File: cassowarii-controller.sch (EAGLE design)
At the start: 17 parts, among them J1 Power, J2 2-PIN_2MM-H, J3 2-PIN_2MM-H, U1 ATTiny85

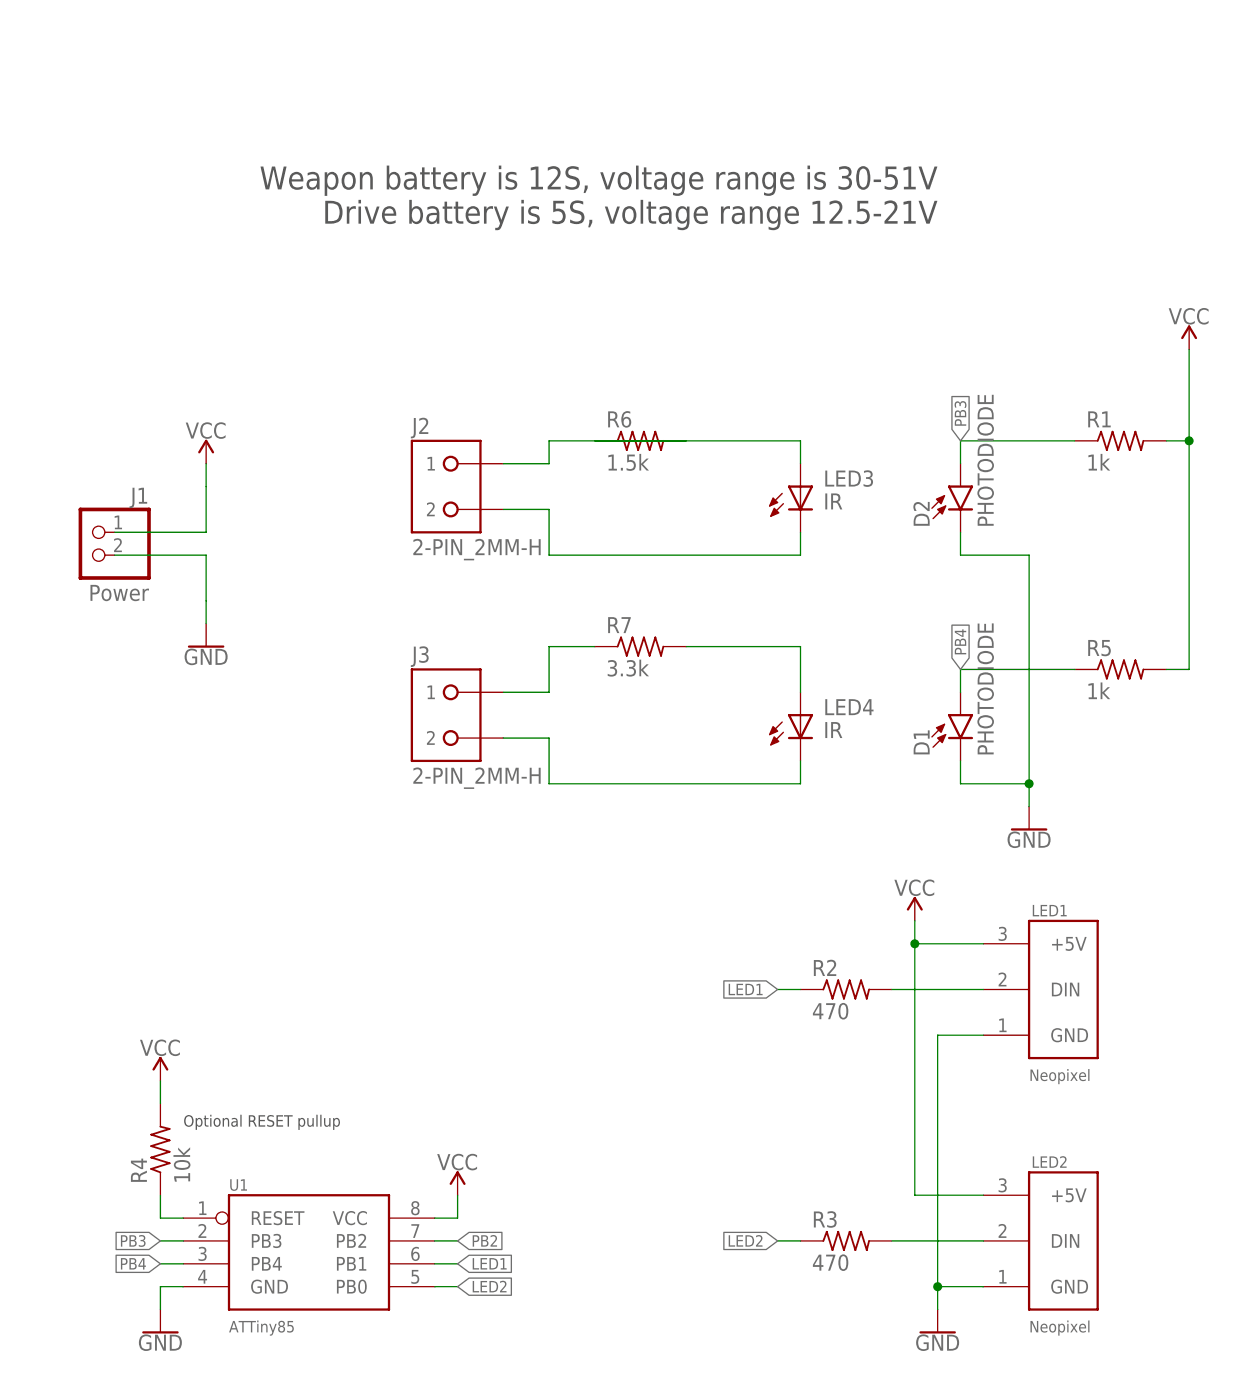
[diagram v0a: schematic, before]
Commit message: New version of Cassowarii controller with proper optoisolators
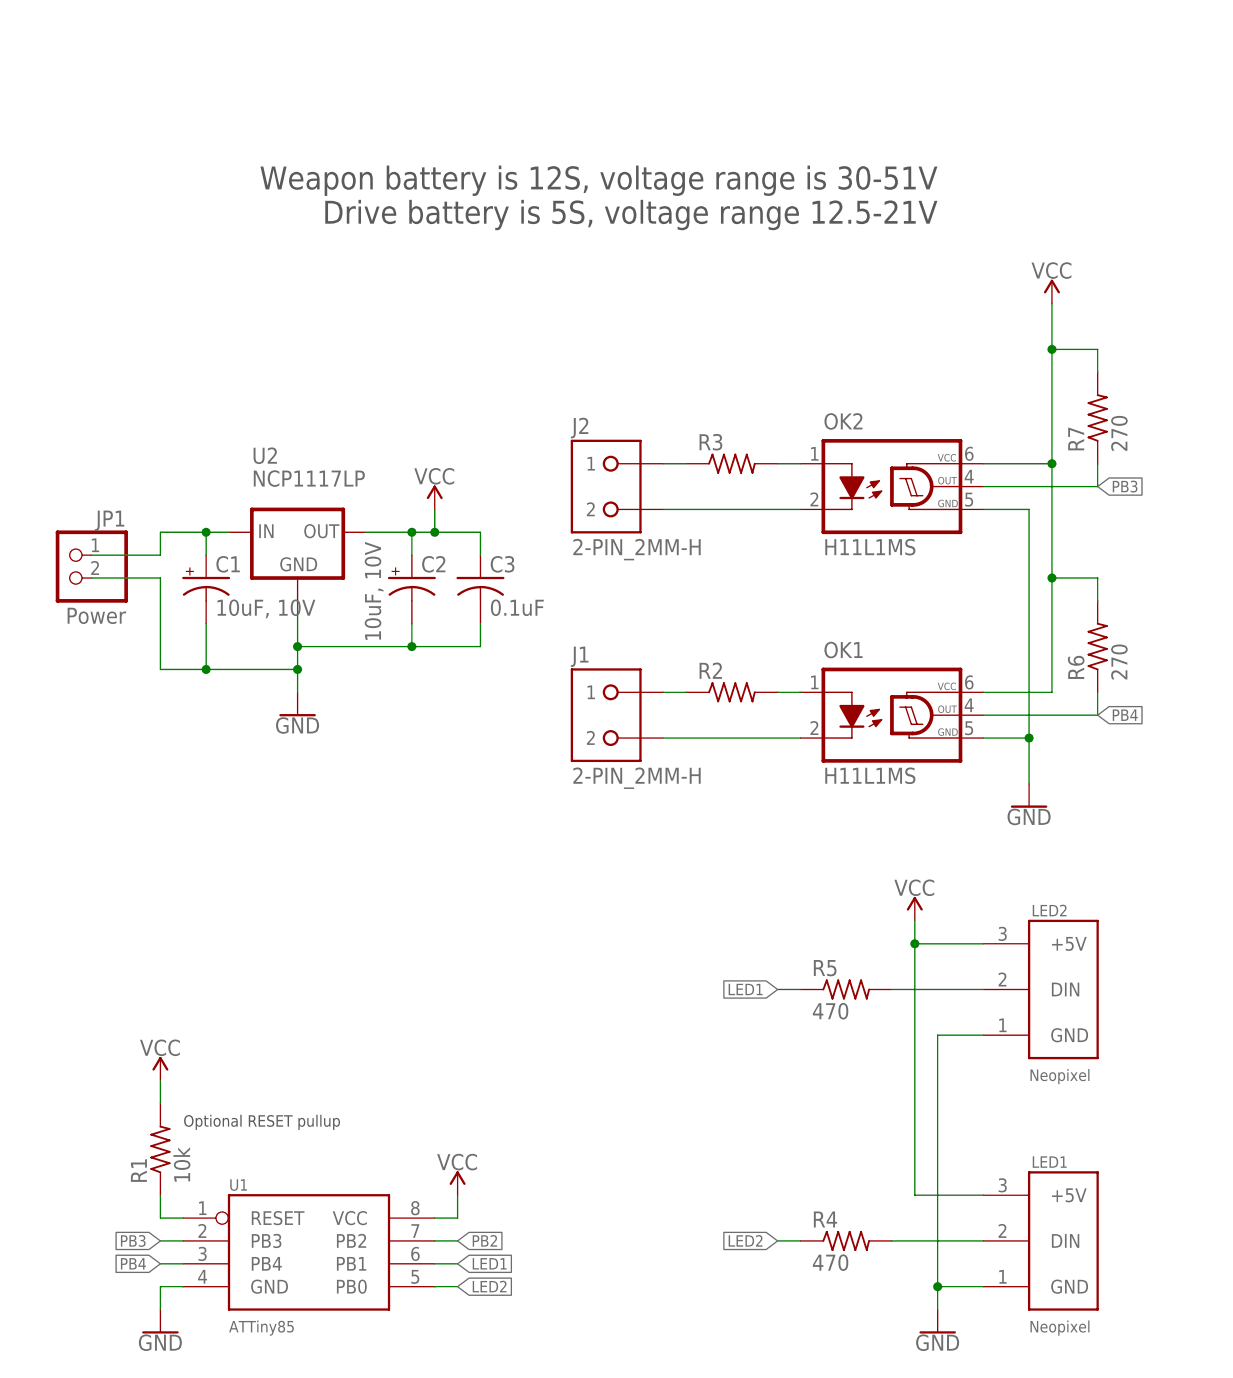
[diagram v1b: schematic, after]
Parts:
- removed D1, D2: PHOTODIODE, JoshCustom:PHOTODIODE
- removed J3: 2-PIN_2MM-H, RoboJackets-Connectors:2-PIN_2MM-H
- removed LED3, LED4: IR, JoshCustom:LED
- added C1, C2: 10uF, 10V, resistor:CPOL-USE1.8-4
- added C3: 0.1uF, resistor:C-USC0805
- added JP1: Power, pinhead:PINHD-1X2
- added OK1, OK2: H11L1MS, optocoupler:H11L1MS
- added U2: NCP1117LP, JoshCustom:NCP1117LP
- J1: value Power -> 2-PIN_2MM-H; device pinhead:PINHD-1X2 -> RoboJackets-Connectors:2-PIN_2MM-H
- R1: value 1k -> 10k
- R2, R3: value 470 -> (none); device resistor:R-US_R0805 -> resistor:R-US_0204/2V
- R4: value 10k -> 470
- R5: value 1k -> 470
- R6: value 1.5k -> 270; device resistor:R-US_0204/2V -> resistor:R-US_R0805
- R7: value 3.3k -> 270; device resistor:R-US_0204/2V -> resistor:R-US_R0805
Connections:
- removed net N$4: LED3.A, R6.1
- new net N$10: OK2.A, R3.2
- new net N$11: C1.+, JP1.1, U2.IN
- net GND: now also C1.-, C2.-, C3.2, JP1.2, OK1.GND, OK2.GND, U2.GND; no longer D1.C, D2.C, J1.2
- net LED1: now also R5.1; no longer R2.1
- net LED2: now also R4.1; no longer R3.1
- net N$1: now also LED1.DIN, R4.2; no longer LED2.DIN, R3.2
- net N$2: now also LED2.DIN, R5.2; no longer LED1.DIN, R2.2
- net N$3: now also R3.1; no longer R6.2
- net N$5: now also R1.1; no longer R4.1
- net N$6: now also OK2.C; no longer LED3.K
- net N$7: now also J1.1, R2.1; no longer J3.1, R7.1
- net N$8: now also OK1.A, R2.2; no longer LED4.A, R7.2
- net N$9: now also J1.2, OK1.C; no longer J3.2, LED4.K
- net PB3: now also OK2.OUT, R7.1; no longer D2.A, R1.1
- net PB4: now also OK1.OUT, R6.1; no longer D1.A, R5.1
- net VCC: now also C2.+, C3.1, OK1.VCC, OK2.VCC, R6.2, R7.2, U2.OUT; no longer J1.1, R4.2, R5.2
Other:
- moved on the sheet: J1, J2, LED1, LED2, R1, R2, R3, R4, R5, R6, R7

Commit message: Redesign Cassowarii controller to use SOIC ATTiny85
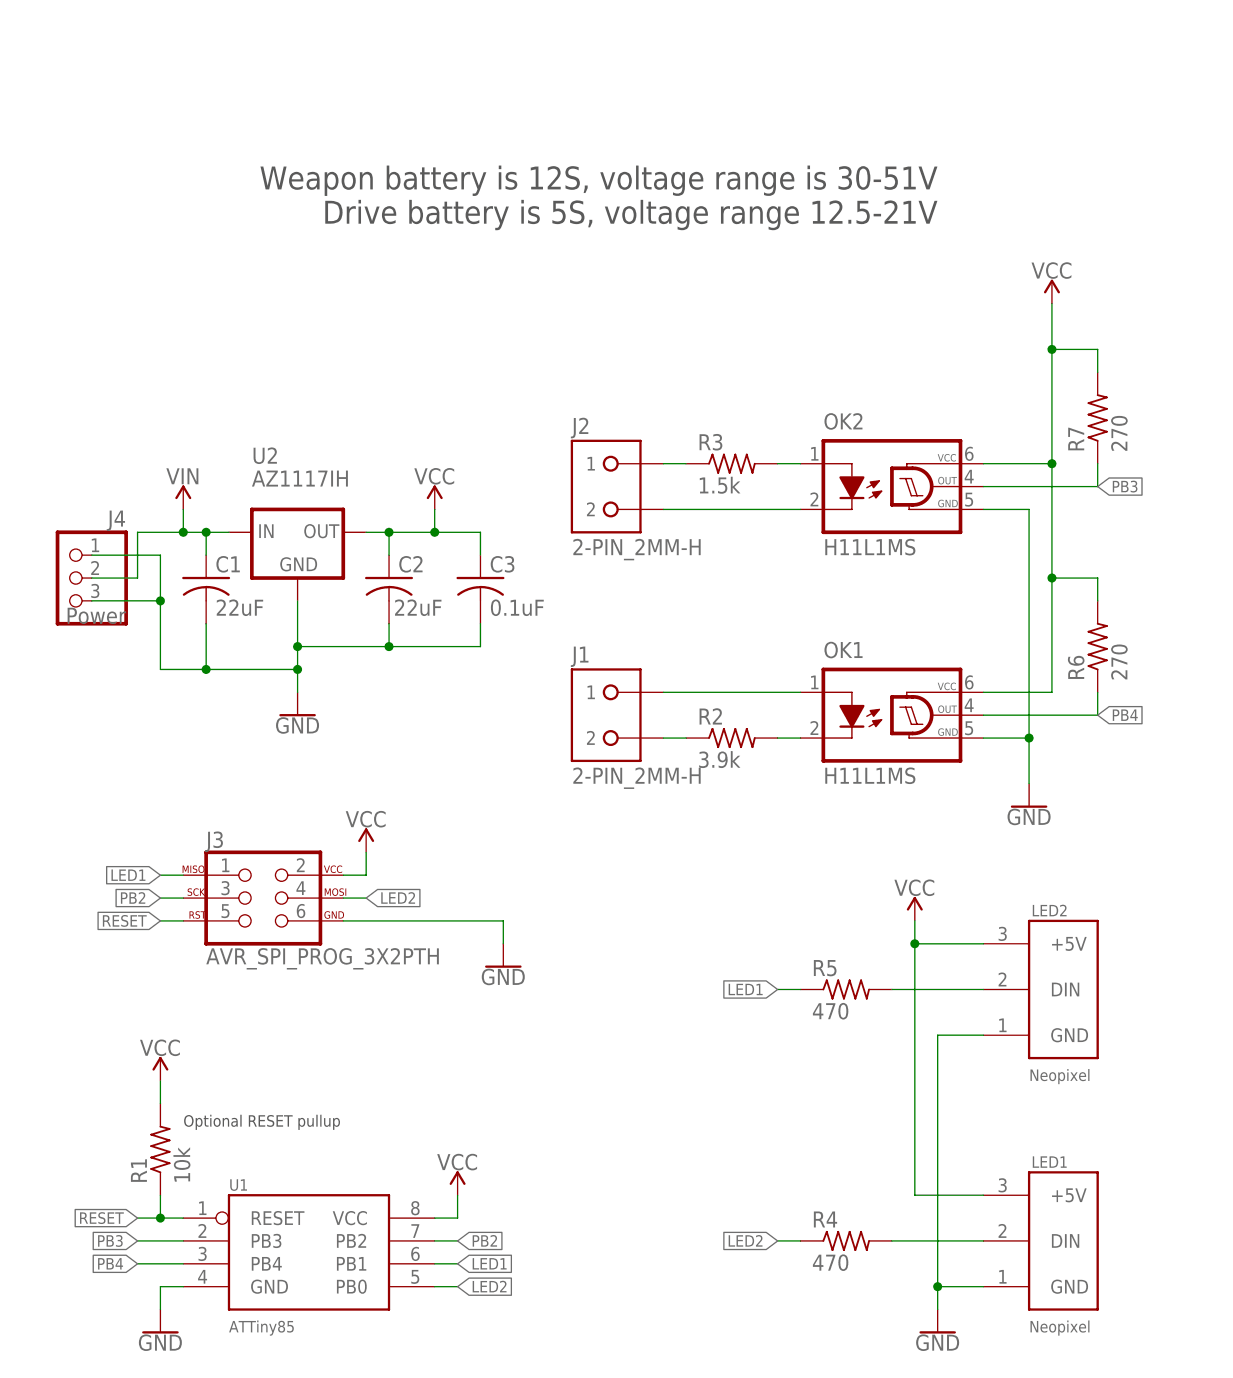
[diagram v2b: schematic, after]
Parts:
- removed JP1: Power, pinhead:PINHD-1X2
- added J3: AVR_SPI_PROG_3X2PTH, SparkFun-Connectors:AVR_SPI_PROG_3X2PTH
- added J4: Power, pinhead:PINHD-1X3
- C1, C2: value 10uF, 10V -> 22uF; device resistor:CPOL-USE1.8-4 -> resistor:C-USC0805
- R2: value (none) -> 3.9k; device resistor:R-US_0204/2V -> resistor:R-US_R0805
- R3: value (none) -> 1.5k; device resistor:R-US_0204/2V -> resistor:R-US_R0805
- U1: device JoshCustom:ATTINY85PDIP8_SOCKET -> JoshCustom:ATTINY85SOIC8
- U2: value NCP1117LP -> AZ1117IH; device JoshCustom:NCP1117LP -> JoshCustom:AZ1117IH
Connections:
- removed net N$11: C1.+, JP1.1, U2.IN
- removed net N$8: OK1.A, R2.2
- removed net N$9: J1.2, OK1.C
- new net N$4: J1.2, R2.1
- new net RESET: J3.5, R1.1, U1.RESET
- new net VIN: C1.1, J4.2, U2.IN
- net GND: now also C1.2, C2.2, J3.6, J4.1, J4.3; no longer C1.-, C2.-, JP1.2
- net LED1: now also J3.1
- net LED2: now also J3.4
- net N$5: now also OK1.C, R2.2; no longer R1.1, U1.RESET
- net N$7: now also OK1.A; no longer R2.1
- net PB2: now also J3.3
- net VCC: now also C2.1, J3.2; no longer C2.+
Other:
- moved on the sheet: R2

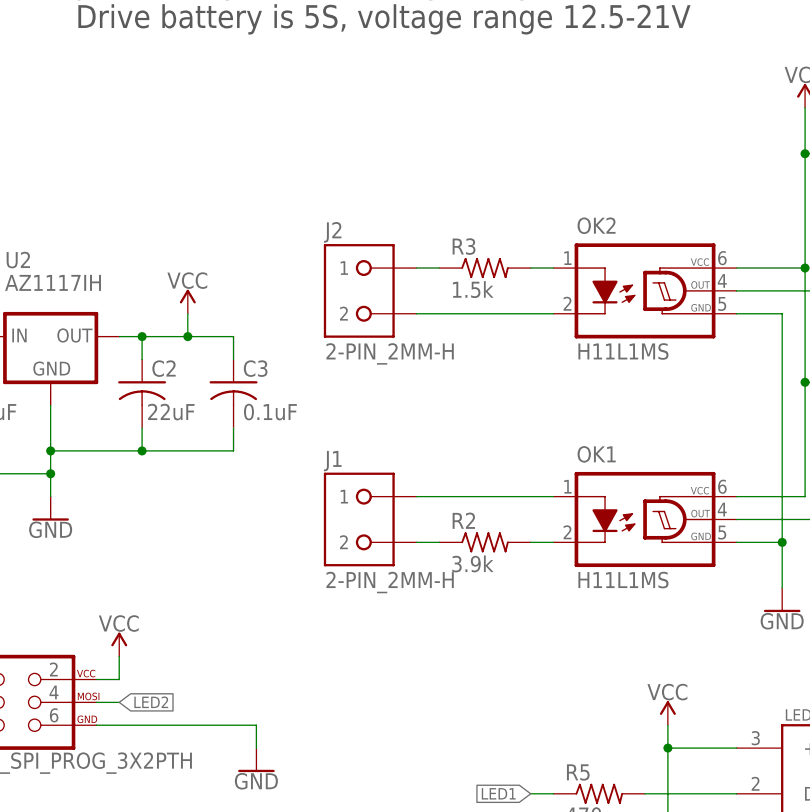
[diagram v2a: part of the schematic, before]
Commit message: Add spots for through hole power resistors
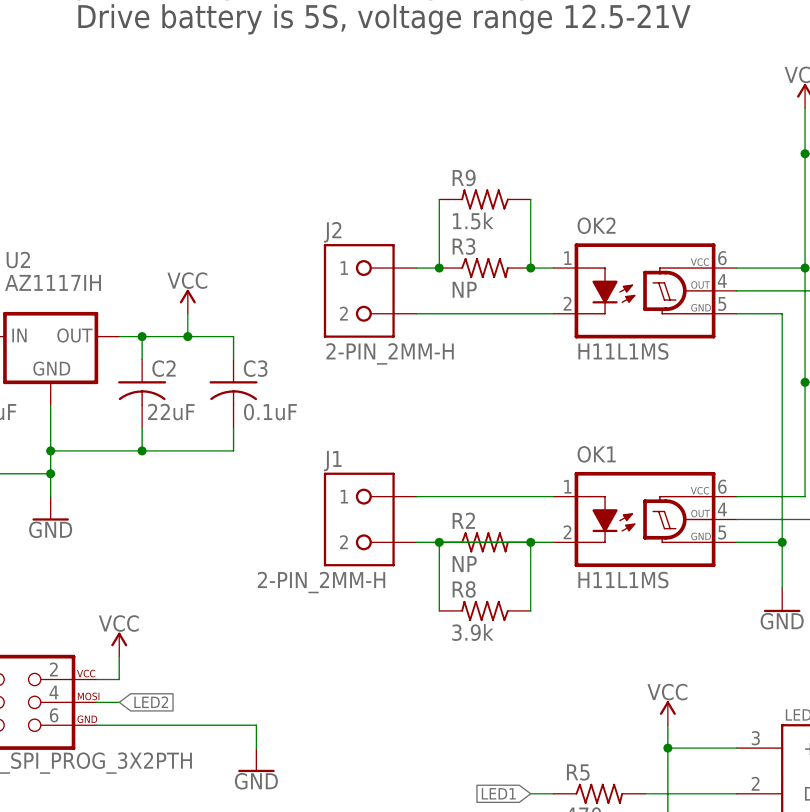
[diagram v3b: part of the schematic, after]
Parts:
- added R8: 3.9k, resistor:R-US_0207/2V
- added R9: 1.5k, resistor:R-US_0207/2V
- R2: value 3.9k -> NP
- R3: value 1.5k -> NP
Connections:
- net N$10: now also R9.1
- net N$3: now also R9.2
- net N$4: now also R2.2, R8.1; no longer R2.1
- net N$5: now also R2.1, R8.2; no longer R2.2
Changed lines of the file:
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@@
 <part name="GND3" library="SparkFun-PowerSymbols" deviceset="GND" device=""/>
 <part name="SUPPLY1" library="SparkFun-PowerSymbols" deviceset="VCC" device=""/>
-<part name="R2" library="resistor" library_urn="urn:adsk.eagle:library:348" deviceset="R-US_" device="R0805" package3d_urn="urn:adsk.eagle:package:23553/2" value="3.9k"/>
+<part name="R2" library="resistor" library_urn="urn:adsk.eagle:library:348" deviceset="R-US_" device="R0805" package3d_urn="urn:adsk.eagle:package:23553/2" value="NP"/>
 <part name="J2" library="RoboJackets-Connectors" deviceset="2-PIN_2MM-*" device="H"/>
 <part name="J1" library="RoboJackets-Connectors" deviceset="2-PIN_2MM-*" device="H"/>
@@
 <part name="OK1" library="optocoupler" library_urn="urn:adsk.eagle:library:320" deviceset="H11L*M" device="S" package3d_urn="urn:adsk.eagle:package:21970/1" technology="1"/>
 <part name="OK2" library="optocoupler" library_urn="urn:adsk.eagle:library:320" deviceset="H11L*M" device="S" package3d_urn="urn:adsk.eagle:package:21970/1" technology="1"/>
-<part name="R3" library="resistor" library_urn="urn:adsk.eagle:library:348" deviceset="R-US_" device="R0805" package3d_urn="urn:adsk.eagle:package:23553/2" value="1.5k"/>
+<part name="R3" library="resistor" library_urn="urn:adsk.eagle:library:348" deviceset="R-US_" device="R0805" package3d_urn="urn:adsk.eagle:package:23553/2" value="NP"/>
 <part name="R7" library="resistor" library_urn="urn:adsk.eagle:library:348" deviceset="R-US_" device="R0805" package3d_urn="urn:adsk.eagle:package:23553/2" value="270"/>
 <part name="R6" library="resistor" library_urn="urn:adsk.eagle:library:348" deviceset="R-US_" device="R0805" package3d_urn="urn:adsk.eagle:package:23553/2" value="270"/>
@@
 <part name="SUPPLY6" library="SparkFun-PowerSymbols" deviceset="VCC" device=""/>
 <part name="SUPPLY7" library="SparkFun-PowerSymbols" deviceset="VIN" device=""/>
+<part name="R8" library="resistor" library_urn="urn:adsk.eagle:library:348" deviceset="R-US_" device="0207/2V" package3d_urn="urn:adsk.eagle:package:23490/1" value="3.9k"/>
+<part name="R9" library="resistor" library_urn="urn:adsk.eagle:library:348" deviceset="R-US_" device="0207/2V" package3d_urn="urn:adsk.eagle:package:23490/1" value="1.5k"/>
 </parts>
 <sheets>
@@
 <instance part="J1" gate="G$1" x="63.5" y="71.12" smashed="yes">
 <attribute name="NAME" x="58.42" y="78.74" size="1.778" layer="95" font="vector" align="top-left"/>
-<attribute name="VALUE" x="58.42" y="63.5" size="1.778" layer="96" font="vector"/>
+<attribute name="VALUE" x="50.8" y="63.5" size="1.778" layer="96" font="vector"/>
 </instance>
 <instance part="GND4" gate="1" x="109.22" y="60.96" smashed="yes">
@@
 <instance part="SUPPLY7" gate="G$1" x="15.24" y="93.98" smashed="yes">
 <attribute name="VALUE" x="15.24" y="96.774" size="1.778" layer="96" align="bottom-center"/>
+</instance>
+<instance part="R8" gate="G$1" x="76.2" y="60.96" smashed="yes" rot="R180">
+<attribute name="NAME" x="72.39" y="62.4586" size="1.778" layer="95"/>
+<attribute name="VALUE" x="72.39" y="57.658" size="1.778" layer="96"/>
+</instance>
+<instance part="R9" gate="G$1" x="76.2" y="106.68" smashed="yes" rot="R180">
+<attribute name="NAME" x="72.39" y="108.1786" size="1.778" layer="95"/>
+<attribute name="VALUE" x="72.39" y="103.378" size="1.778" layer="96"/>
 </instance>
 </instances>
@@
 <wire x1="68.58" y1="99.06" x2="71.12" y2="99.06" width="0.1524" layer="91"/>
 <pinref part="R3" gate="G$1" pin="1"/>
+<pinref part="R9" gate="G$1" pin="2"/>
+<wire x1="71.12" y1="99.06" x2="71.12" y2="106.68" width="0.1524" layer="91"/>
+<junction x="71.12" y="99.06"/>
 </segment>
 </net>
@@
 <pinref part="R3" gate="G$1" pin="2"/>
 <wire x1="81.28" y1="99.06" x2="83.82" y2="99.06" width="0.1524" layer="91"/>
+<pinref part="R9" gate="G$1" pin="1"/>
+<wire x1="81.28" y1="106.68" x2="81.28" y2="99.06" width="0.1524" layer="91"/>
+<junction x="81.28" y="99.06"/>
 </segment>
 </net>
@@
 <segment>
 <pinref part="J1" gate="G$1" pin="2"/>
+<pinref part="R2" gate="G$1" pin="2"/>
+<wire x1="68.58" y1="68.58" x2="81.28" y2="68.58" width="0.1524" layer="91"/>
+<pinref part="R8" gate="G$1" pin="1"/>
+<wire x1="81.28" y1="60.96" x2="81.28" y2="68.58" width="0.1524" layer="91"/>
+<junction x="81.28" y="68.58"/>
+</segment>
+</net>
+<net name="N$5" class="0">
+<segment>
 <pinref part="R2" gate="G$1" pin="1"/>
-<wire x1="68.58" y1="68.58" x2="71.12" y2="68.58" width="0.1524" layer="91"/>
-</segment>
-</net>
-<net name="N$5" class="0">
-<segment>
-<pinref part="R2" gate="G$1" pin="2"/>
 <pinref part="OK1" gate="G$1" pin="C"/>
-<wire x1="81.28" y1="68.58" x2="83.82" y2="68.58" width="0.1524" layer="91"/>
+<wire x1="71.12" y1="68.58" x2="83.82" y2="68.58" width="0.1524" layer="91"/>
+<pinref part="R8" gate="G$1" pin="2"/>
+<wire x1="71.12" y1="68.58" x2="71.12" y2="60.96" width="0.1524" layer="91"/>
+<junction x="71.12" y="68.58"/>
 </segment>
 </net>
@@
 </sheet>
 </sheets>
-<errors>
-</errors>
 </schematic>
 </drawing>
